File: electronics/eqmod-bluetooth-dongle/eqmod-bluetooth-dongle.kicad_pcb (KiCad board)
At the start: 4 copper layers, 47 x 23.8 mm, 6 parts

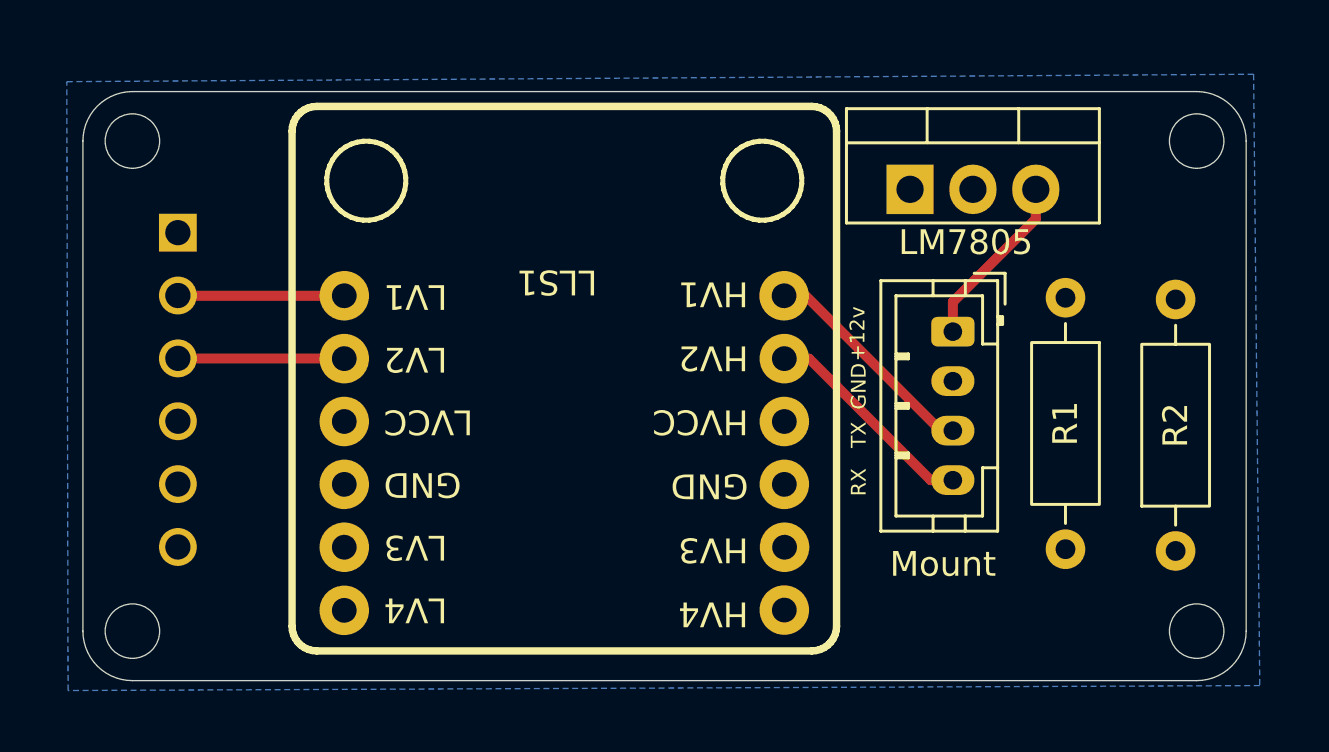
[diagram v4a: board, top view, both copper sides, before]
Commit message: Fix: Use connector that can be sourced from supplier (#6)
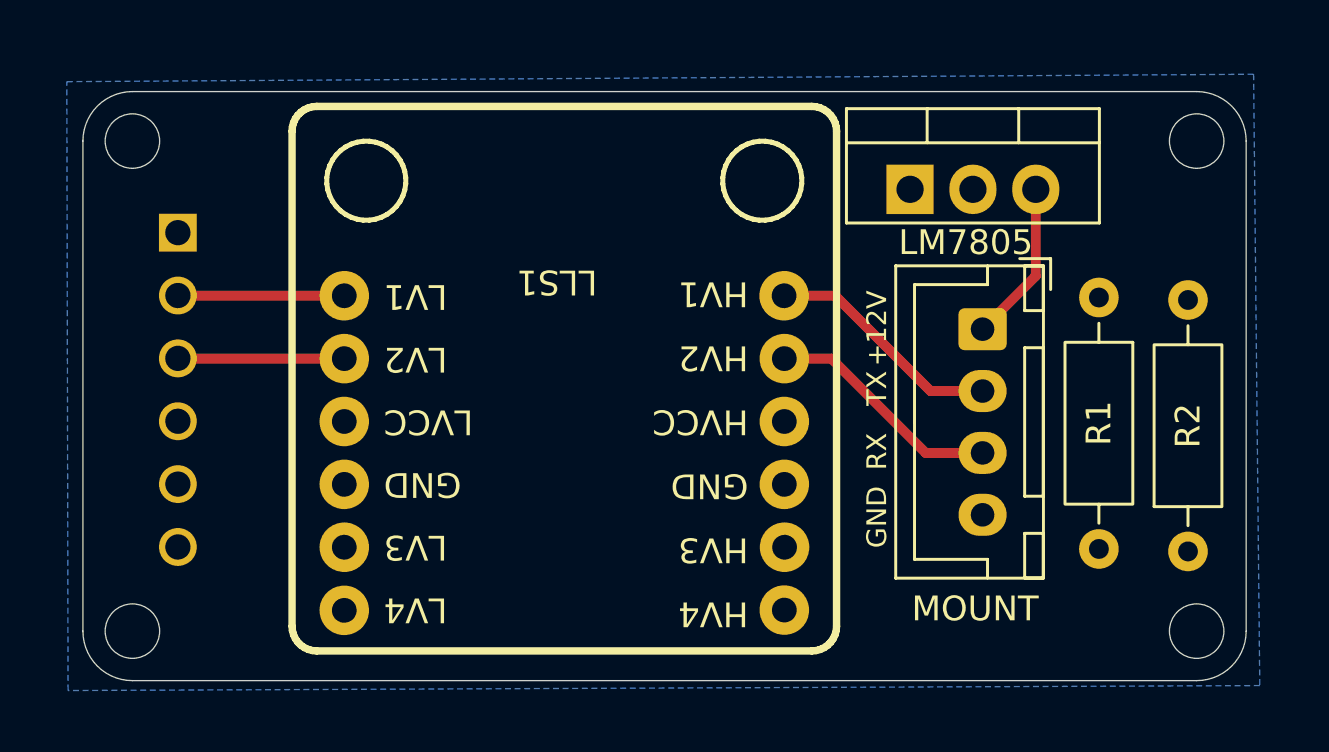
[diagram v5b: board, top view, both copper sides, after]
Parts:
- MOUNT: renamed from Mount; footprint Connector_JST:JST_PH_B4B-PH-K_1x04_P2.00mm_Vertical -> Connector_JST:JST_XH_B4B-XH-A_1x04_P2.50mm_Vertical
- moved R1 1.35 mm to (145.1, 91.2)
- moved MOUNT 1.20 mm to (140.4, 92.5)
- moved R2 0.50 mm to (148.7, 101.5)
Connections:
- net +3V3 renamed +3.3V
- net MOUNT_+12V renamed +12V
- MOUNT pad 2: GND -> MOUNT_TX
- MOUNT pad 3: MOUNT_TX -> MOUNT_RX
- MOUNT pad 4: MOUNT_RX -> GND
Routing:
- net +12V: track 8.74 -> 6.54 mm
- net MOUNT_RX: track 8.84 -> 9.59 mm

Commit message: Let's go print some PCB (#7)
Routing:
- added copper zone on F.Cu, net +3.3V
- added copper zone on F.Cu, net +5V
- removed copper zone on In1.Cu, net +3.3V
- removed copper zone on In2.Cu, net +5V
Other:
- copper layers 4 -> 2
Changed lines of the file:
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@@
 	(layers
 		(0 "F.Cu" signal)
-		(4 "In1.Cu" signal)
-		(6 "In2.Cu" signal)
 		(2 "B.Cu" signal)
 		(9 "F.Adhes" user "F.Adhesive")
@@
 			)
 			(layer "dielectric 1"
-				(type "prepreg")
-				(thickness 0.1)
-				(material "FR4")
-				(epsilon_r 4.5)
-				(loss_tangent 0.02)
-			)
-			(layer "In1.Cu"
-				(type "copper")
-				(thickness 0.035)
-			)
-			(layer "dielectric 2"
 				(type "core")
-				(thickness 1.24)
-				(material "FR4")
-				(epsilon_r 4.5)
-				(loss_tangent 0.02)
-			)
-			(layer "In2.Cu"
-				(type "copper")
-				(thickness 0.035)
-			)
-			(layer "dielectric 3"
-				(type "prepreg")
-				(thickness 0.1)
+				(thickness 1.51)
 				(material "FR4")
 				(epsilon_r 4.5)
@@
 	)
 	(zone
-		(net 5)
-		(net_name "GND")
-		(layer "B.Cu")
+		(net 6)
+		(net_name "+5V")
+		(layer "F.Cu")
 		(hatch edge 0.5)
+		(priority 2)
 		(connect_pads
 			(clearance 0.5)
@@
 		(polygon
 			(pts
-				(xy 103.45 107.1) (xy 103.4 82.5) (xy 151.35 82.2) (xy 151.6 106.9)
+				(xy 110.4 107.5) (xy 102.8 107.5) (xy 102.7 81.6) (xy 152.4 81.6) (xy 151.8 98.1) (xy 128.8 98.3)
+				(xy 117 88.7) (xy 113.2 88.7) (xy 110.5 89.8)
 			)
 		)
@@
 		(net 11)
 		(net_name "+3.3V")
-		(layer "In1.Cu")
+		(layer "F.Cu")
 		(hatch edge 0.5)
 		(priority 1)
@@
 		(polygon
 			(pts
-				(xy 102.9 82.1) (xy 152.05 81.85) (xy 152.2 107.4) (xy 102.9 107.65)
+				(xy 110.4 107.5) (xy 110.5 89.8) (xy 113.2 88.7) (xy 117 88.7) (xy 128.8 98.3) (xy 136.5 98.3) (xy 151.8 98.1)
+				(xy 151.8 107.6)
 			)
 		)
 	)
 	(zone
-		(net 6)
-		(net_name "+5V")
-		(layer "In2.Cu")
+		(net 5)
+		(net_name "GND")
+		(layer "B.Cu")
 		(hatch edge 0.5)
-		(priority 2)
 		(connect_pads
 			(clearance 0.5)
@@
 		(polygon
 			(pts
-				(xy 102.3 81.45) (xy 152.6 81.1) (xy 152.65 107.85) (xy 102.3 108.05)
+				(xy 103.45 107.1) (xy 103.4 82.5) (xy 151.35 82.2) (xy 151.6 106.9)
 			)
 		)
